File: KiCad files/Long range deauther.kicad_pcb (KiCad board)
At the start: 2 copper layers, 43 x 16 mm, 32 parts, among them J1 USB_A, Q1 BC847, Q2 BC847, SW1 SW_RST, SW2 SW_Flash, U1 AP2112-3.3, U2 FT231XS, U3 ESP-WROOM-02U

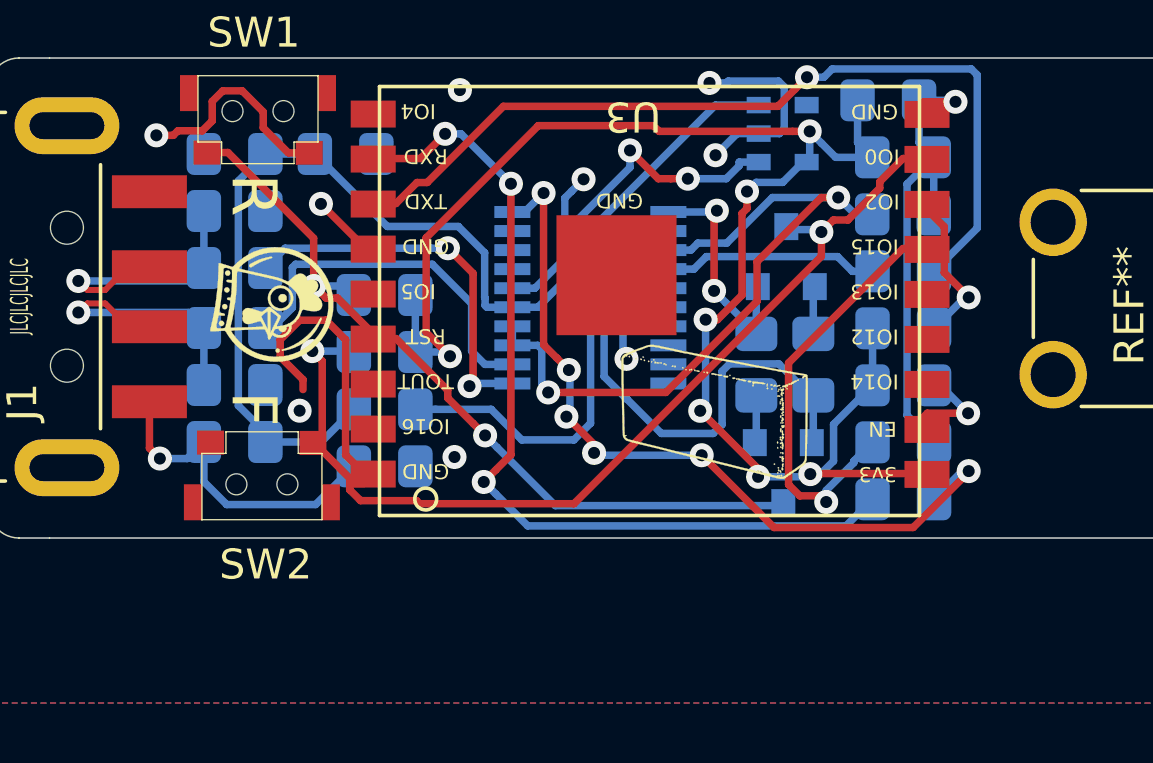
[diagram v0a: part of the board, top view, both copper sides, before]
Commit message: fixed idiote trace mistake
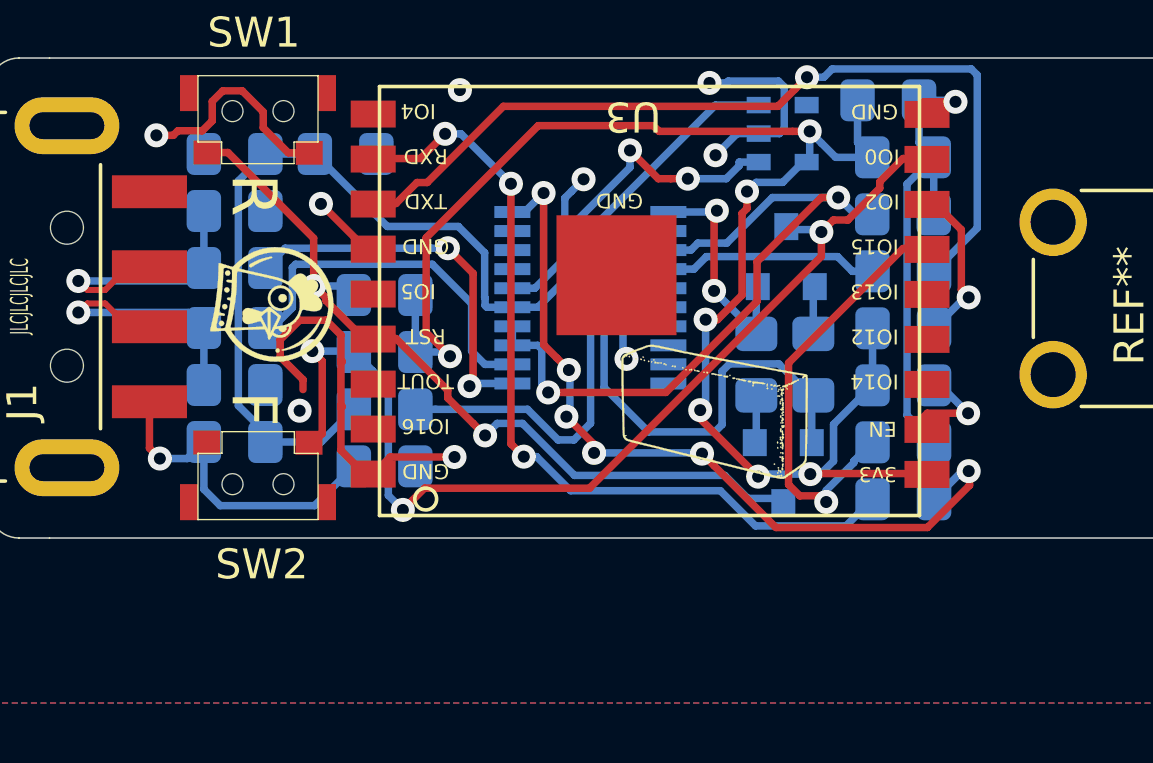
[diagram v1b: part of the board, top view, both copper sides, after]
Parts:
- moved SW2 0.13 mm to (134.9, 89.2)
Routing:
- net GND: track 51.0 -> 54.0 mm
- net Net-(R7-Pad1): track 29.4 -> 27.4 mm
- net E_IO0: track 32.3 -> 34.3 mm, vias 2 -> 3
- net E_IO2: track 5.69 -> 6.26 mm
